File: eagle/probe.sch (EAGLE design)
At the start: 14 parts

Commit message: probe pcb v1
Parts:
- removed LED10, LED11, LED12, LED13, LED14, LED4, LED5, LED6, LED7, LED8, LED9: (no value), led:LED5MM
- added TO1, TO2, TO3, TO4, TO5, TO6: (no value), general:LED5MM
- UV1, UV2, UV3: device led:LED5MM -> general:LED5MM
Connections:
- new net N$2: TO1.C, TO2.C, TO3.C, TO4.C, TO5.C, TO6.C
- net N$1: now also TO1.A, TO2.A, TO3.A, TO4.A, TO5.A, TO6.A
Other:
- moved on the sheet: UV1, UV2, UV3

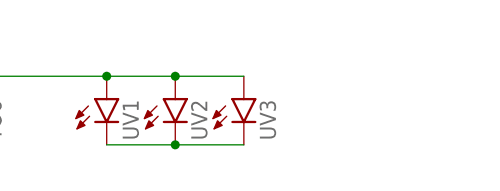
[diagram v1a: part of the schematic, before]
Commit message: Updated probe and rear eagle files
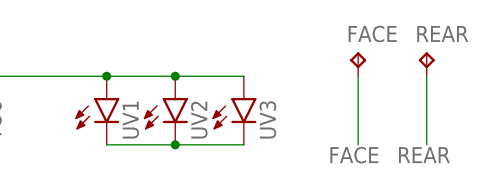
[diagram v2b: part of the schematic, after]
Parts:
- added FACE, REAR: TPTP10R, testpad:TPTP10R
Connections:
- new net FACE: FACE.TP
- new net REAR: REAR.TP
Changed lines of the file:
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@@
 </variantdefs>
 <classes>
-<class number="0" name="default" width="0.2032" drill="0">
+<class number="0" name="default" width="0.1524" drill="0">
+</class>
+<class number="1" name="thick" width="0.508" drill="0">
 </class>
 </classes>
@@
 <part name="UV2" library="general" deviceset="LED" device="5MM" package3d_urn="urn:adsk.eagle:package:15799/2"/>
 <part name="UV3" library="general" deviceset="LED" device="5MM" package3d_urn="urn:adsk.eagle:package:15799/2"/>
+<part name="FACE" library="testpad" library_urn="urn:adsk.eagle:library:385" deviceset="TP" device="TP10R" package3d_urn="urn:adsk.eagle:package:27959/1"/>
+<part name="REAR" library="testpad" library_urn="urn:adsk.eagle:library:385" deviceset="TP" device="TP10R" package3d_urn="urn:adsk.eagle:package:27959/1"/>
 </parts>
 <sheets>
@@
 <attribute name="NAME" x="41.656" y="46.228" size="1.778" layer="95" rot="R90"/>
 <attribute name="VALUE" x="43.815" y="46.228" size="1.778" layer="96" rot="R90"/>
+</instance>
+<instance part="FACE" gate="G$1" x="50.8" y="55.88" smashed="yes">
+<attribute name="NAME" x="49.53" y="57.15" size="1.778" layer="95"/>
+<attribute name="TP_SIGNAL_NAME" x="52.07" y="54.61" size="1.778" layer="97"/>
+</instance>
+<instance part="REAR" gate="G$1" x="58.42" y="55.88" smashed="yes">
+<attribute name="NAME" x="57.15" y="57.15" size="1.778" layer="95"/>
+<attribute name="TP_SIGNAL_NAME" x="59.69" y="54.61" size="1.778" layer="97"/>
 </instance>
 </instances>
@@
 </segment>
 </net>
+<net name="FACE" class="1">
+<segment>
+<pinref part="FACE" gate="G$1" pin="TP"/>
+<wire x1="50.8" y1="53.34" x2="50.8" y2="45.72" width="0.1524" layer="91"/>
+<label x="47.498" y="43.688" size="1.778" layer="95"/>
+</segment>
+</net>
+<net name="REAR" class="0">
+<segment>
+<pinref part="REAR" gate="G$1" pin="TP"/>
+<wire x1="58.42" y1="53.34" x2="58.42" y2="45.72" width="0.1524" layer="91"/>
+<label x="55.118" y="43.688" size="1.778" layer="95"/>
+</segment>
+</net>
 </nets>
 </sheet>
@@
 </drawing>
 <compatibility>
+<note version="8.2" severity="warning">
+Since Version 8.2, EAGLE supports online libraries. The ids
+of those online libraries will not be understood (or retained)
+with this version.
+</note>
 <note version="8.3" severity="warning">
 Since Version 8.3, EAGLE supports URNs for individual library

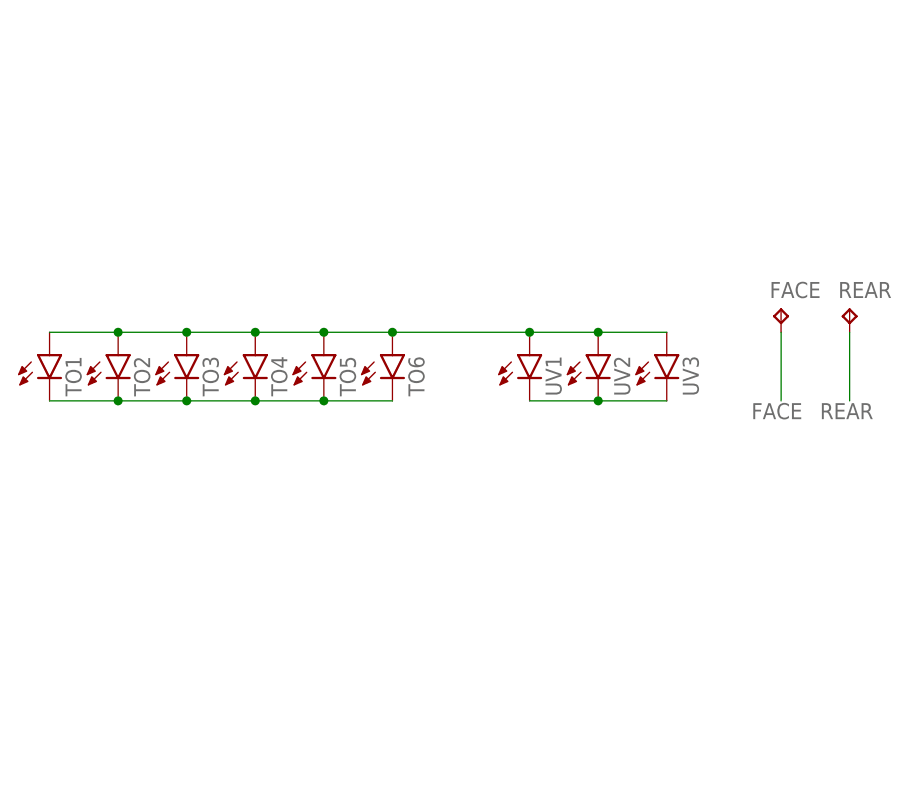
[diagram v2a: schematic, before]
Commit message: Re-organise eagle folder
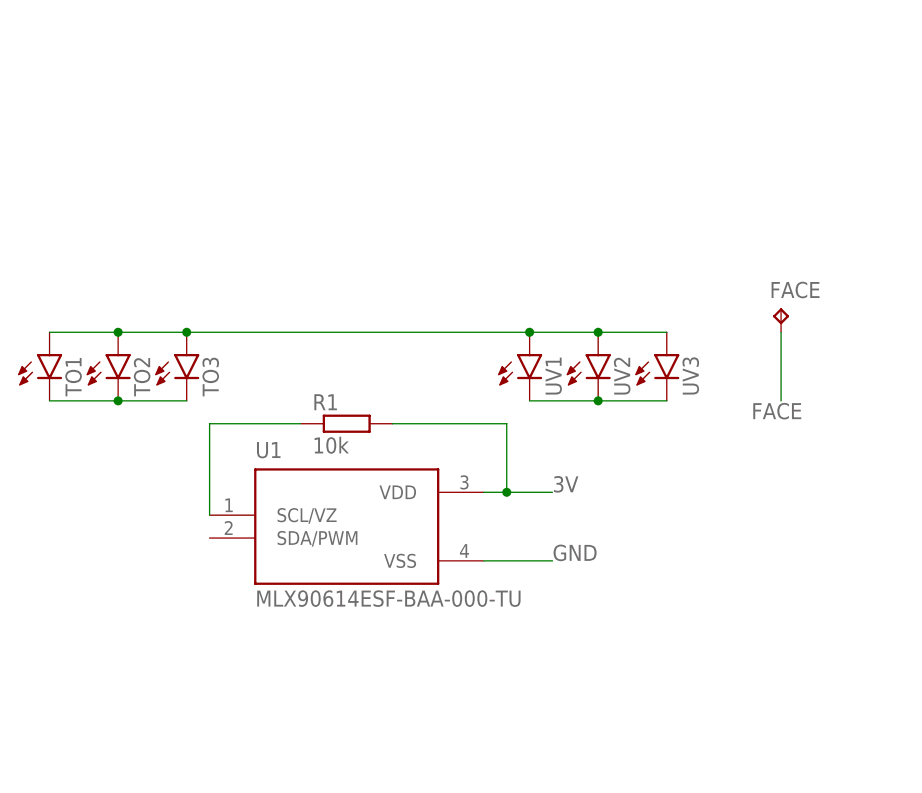
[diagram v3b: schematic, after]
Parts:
- removed REAR: TPTP10R, testpad:TPTP10R
- removed TO4, TO5, TO6: (no value), general:LED5MM
- added R1: 10k, resistor:R-EU_R0805
- added U1: MLX90614ESF-BAA-000-TU, MLX90614ESF-BAA-000-TU:MLX90614ESF-BAA-000-TU
- FACE: value TPTP10R -> TPTP14R; device testpad:TPTP10R -> testpad:TPTP14R
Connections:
- removed net N$1: TO1.A, TO2.A, TO3.A, TO4.A, TO5.A, TO6.A, UV1.A, UV2.A, UV3.A
- removed net REAR: REAR.TP
- new net 3V: R1.2, TO1.A, TO2.A, TO3.A, U1.VDD, UV1.A, UV2.A, UV3.A
- new net GND: U1.VSS
- new net SCL: R1.1, U1.SCL/VZ
- net N$2: no longer TO4.C, TO5.C, TO6.C
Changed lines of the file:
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@@
 </variantdefs>
 <classes>
-<class number="0" name="default" width="0.1524" drill="0">
-</class>
-<class number="1" name="thick" width="0.508" drill="0">
+<class number="0" name="default" width="0" drill="0">
 </class>
 </classes>
@@
 <part name="TO2" library="general" deviceset="LED" device="5MM" package3d_urn="urn:adsk.eagle:package:15799/2"/>
 <part name="TO3" library="general" deviceset="LED" device="5MM" package3d_urn="urn:adsk.eagle:package:15799/2"/>
-<part name="TO4" library="general" deviceset="LED" device="5MM" package3d_urn="urn:adsk.eagle:package:15799/2"/>
-<part name="TO5" library="general" deviceset="LED" device="5MM" package3d_urn="urn:adsk.eagle:package:15799/2"/>
-<part name="TO6" library="general" deviceset="LED" device="5MM" package3d_urn="urn:adsk.eagle:package:15799/2"/>
 <part name="UV1" library="general" deviceset="LED" device="5MM" package3d_urn="urn:adsk.eagle:package:15799/2"/>
 <part name="UV2" library="general" deviceset="LED" device="5MM" package3d_urn="urn:adsk.eagle:package:15799/2"/>
 <part name="UV3" library="general" deviceset="LED" device="5MM" package3d_urn="urn:adsk.eagle:package:15799/2"/>
-<part name="FACE" library="testpad" library_urn="urn:adsk.eagle:library:385" deviceset="TP" device="TP10R" package3d_urn="urn:adsk.eagle:package:27959/1"/>
-<part name="REAR" library="testpad" library_urn="urn:adsk.eagle:library:385" deviceset="TP" device="TP10R" package3d_urn="urn:adsk.eagle:package:27959/1"/>
+<part name="U1" library="MLX90614ESF-BAA-000-TU" deviceset="MLX90614ESF-BAA-000-TU" device=""/>
+<part name="FACE" library="testpad" library_urn="urn:adsk.eagle:library:385" deviceset="TP" device="TP14R" package3d_urn="urn:adsk.eagle:package:27966/1"/>
+<part name="R1" library="resistor" library_urn="urn:adsk.eagle:library:348" deviceset="R-EU_" device="R0805" package3d_urn="urn:adsk.eagle:package:23553/2" value="10k"/>
 </parts>
 <sheets>
@@
 <attribute name="VALUE" x="-9.525" y="46.228" size="1.778" layer="96" rot="R90"/>
 </instance>
-<instance part="TO4" gate="G$1" x="-7.62" y="50.8" smashed="yes">
-<attribute name="NAME" x="-4.064" y="46.228" size="1.778" layer="95" rot="R90"/>
-<attribute name="VALUE" x="-1.905" y="46.228" size="1.778" layer="96" rot="R90"/>
-</instance>
-<instance part="TO5" gate="G$1" x="0" y="50.8" smashed="yes">
-<attribute name="NAME" x="3.556" y="46.228" size="1.778" layer="95" rot="R90"/>
-<attribute name="VALUE" x="5.715" y="46.228" size="1.778" layer="96" rot="R90"/>
-</instance>
-<instance part="TO6" gate="G$1" x="7.62" y="50.8" smashed="yes">
-<attribute name="NAME" x="11.176" y="46.228" size="1.778" layer="95" rot="R90"/>
-<attribute name="VALUE" x="13.335" y="46.228" size="1.778" layer="96" rot="R90"/>
-</instance>
 <instance part="UV1" gate="G$1" x="22.86" y="50.8" smashed="yes">
 <attribute name="NAME" x="26.416" y="46.228" size="1.778" layer="95" rot="R90"/>
@@
 <attribute name="VALUE" x="43.815" y="46.228" size="1.778" layer="96" rot="R90"/>
 </instance>
+<instance part="U1" gate="G$1" x="2.54" y="33.02" smashed="yes">
+<attribute name="NAME" x="-7.62" y="39.37" size="1.778" layer="95"/>
+<attribute name="VALUE" x="-7.62" y="22.86" size="1.778" layer="96"/>
+</instance>
 <instance part="FACE" gate="G$1" x="50.8" y="55.88" smashed="yes">
 <attribute name="NAME" x="49.53" y="57.15" size="1.778" layer="95"/>
 <attribute name="TP_SIGNAL_NAME" x="52.07" y="54.61" size="1.778" layer="97"/>
 </instance>
-<instance part="REAR" gate="G$1" x="58.42" y="55.88" smashed="yes">
-<attribute name="NAME" x="57.15" y="57.15" size="1.778" layer="95"/>
-<attribute name="TP_SIGNAL_NAME" x="59.69" y="54.61" size="1.778" layer="97"/>
+<instance part="R1" gate="G$1" x="2.54" y="43.18" smashed="yes">
+<attribute name="NAME" x="-1.27" y="44.6786" size="1.778" layer="95"/>
+<attribute name="VALUE" x="-1.27" y="39.878" size="1.778" layer="96"/>
 </instance>
 </instances>
@@
 </busses>
 <nets>
-<net name="N$1" class="0">
-<segment>
-<pinref part="TO1" gate="G$1" pin="A"/>
-<pinref part="TO2" gate="G$1" pin="A"/>
-<wire x1="-30.48" y1="53.34" x2="-22.86" y2="53.34" width="0.1524" layer="91"/>
-<pinref part="TO3" gate="G$1" pin="A"/>
-<wire x1="-22.86" y1="53.34" x2="-15.24" y2="53.34" width="0.1524" layer="91"/>
-<junction x="-22.86" y="53.34"/>
-<pinref part="TO4" gate="G$1" pin="A"/>
-<wire x1="-15.24" y1="53.34" x2="-7.62" y2="53.34" width="0.1524" layer="91"/>
-<junction x="-15.24" y="53.34"/>
-<pinref part="TO5" gate="G$1" pin="A"/>
-<wire x1="-7.62" y1="53.34" x2="0" y2="53.34" width="0.1524" layer="91"/>
-<junction x="-7.62" y="53.34"/>
-<pinref part="TO6" gate="G$1" pin="A"/>
-<wire x1="0" y1="53.34" x2="7.62" y2="53.34" width="0.1524" layer="91"/>
-<junction x="0" y="53.34"/>
-<pinref part="UV1" gate="G$1" pin="A"/>
-<pinref part="UV2" gate="G$1" pin="A"/>
-<wire x1="22.86" y1="53.34" x2="30.48" y2="53.34" width="0.1524" layer="91"/>
-<pinref part="UV3" gate="G$1" pin="A"/>
-<wire x1="30.48" y1="53.34" x2="38.1" y2="53.34" width="0.1524" layer="91"/>
-<junction x="30.48" y="53.34"/>
-<wire x1="7.62" y1="53.34" x2="22.86" y2="53.34" width="0.1524" layer="91"/>
-<junction x="7.62" y="53.34"/>
-<junction x="22.86" y="53.34"/>
-</segment>
-</net>
 <net name="N$2" class="0">
 <segment>
@@
 <wire x1="-22.86" y1="45.72" x2="-15.24" y2="45.72" width="0.1524" layer="91"/>
 <junction x="-22.86" y="45.72"/>
-<pinref part="TO4" gate="G$1" pin="C"/>
-<wire x1="-15.24" y1="45.72" x2="-7.62" y2="45.72" width="0.1524" layer="91"/>
-<junction x="-15.24" y="45.72"/>
-<pinref part="TO5" gate="G$1" pin="C"/>
-<wire x1="-7.62" y1="45.72" x2="0" y2="45.72" width="0.1524" layer="91"/>
-<junction x="-7.62" y="45.72"/>
-<pinref part="TO6" gate="G$1" pin="C"/>
-<wire x1="0" y1="45.72" x2="7.62" y2="45.72" width="0.1524" layer="91"/>
-<junction x="0" y="45.72"/>
 </segment>
 </net>
@@
 </segment>
 </net>
-<net name="FACE" class="1">
+<net name="FACE" class="0">
 <segment>
-<pinref part="FACE" gate="G$1" pin="TP"/>
 <wire x1="50.8" y1="53.34" x2="50.8" y2="45.72" width="0.1524" layer="91"/>
 <label x="47.498" y="43.688" size="1.778" layer="95"/>
+<pinref part="FACE" gate="G$1" pin="TP"/>
 </segment>
 </net>
-<net name="REAR" class="0">
+<net name="GND" class="0">
 <segment>
-<pinref part="REAR" gate="G$1" pin="TP"/>
-<wire x1="58.42" y1="53.34" x2="58.42" y2="45.72" width="0.1524" layer="91"/>
-<label x="55.118" y="43.688" size="1.778" layer="95"/>
+<pinref part="U1" gate="G$1" pin="VSS"/>
+<wire x1="17.78" y1="27.94" x2="25.4" y2="27.94" width="0.1524" layer="91"/>
+<label x="25.4" y="27.94" size="1.778" layer="95"/>
 </segment>
 </net>
+<net name="3V" class="0">
+<segment>
+<pinref part="U1" gate="G$1" pin="VDD"/>
+<wire x1="17.78" y1="35.56" x2="20.32" y2="35.56" width="0.1524" layer="91"/>
+<label x="25.4" y="35.56" size="1.778" layer="95"/>
+<pinref part="R1" gate="G$1" pin="2"/>
+<wire x1="20.32" y1="35.56" x2="25.4" y2="35.56" width="0.1524" layer="91"/>
+<wire x1="7.62" y1="43.18" x2="20.32" y2="43.18" width="0.1524" layer="91"/>
+<wire x1="20.32" y1="43.18" x2="20.32" y2="35.56" width="0.1524" layer="91"/>
+<junction x="20.32" y="35.56"/>
+</segment>
+<segment>
+<pinref part="TO1" gate="G$1" pin="A"/>
+<pinref part="TO2" gate="G$1" pin="A"/>
+<wire x1="-30.48" y1="53.34" x2="-22.86" y2="53.34" width="0.1524" layer="91"/>
+<pinref part="TO3" gate="G$1" pin="A"/>
+<wire x1="-22.86" y1="53.34" x2="-15.24" y2="53.34" width="0.1524" layer="91"/>
+<junction x="-22.86" y="53.34"/>
+<junction x="-15.24" y="53.34"/>
+<pinref part="UV1" gate="G$1" pin="A"/>
+<pinref part="UV2" gate="G$1" pin="A"/>
+<wire x1="22.86" y1="53.34" x2="30.48" y2="53.34" width="0.1524" layer="91"/>
+<pinref part="UV3" gate="G$1" pin="A"/>
+<wire x1="30.48" y1="53.34" x2="38.1" y2="53.34" width="0.1524" layer="91"/>
+<junction x="30.48" y="53.34"/>
+<wire x1="-15.24" y1="53.34" x2="22.86" y2="53.34" width="0.1524" layer="91"/>
+<junction x="22.86" y="53.34"/>
+</segment>
+</net>
+<net name="SCL" class="0">
+<segment>
+<pinref part="U1" gate="G$1" pin="SCL/VZ"/>
+<wire x1="-12.7" y1="33.02" x2="-12.7" y2="43.18" width="0.1524" layer="91"/>
+<pinref part="R1" gate="G$1" pin="1"/>
+<wire x1="-12.7" y1="43.18" x2="-2.54" y2="43.18" width="0.1524" layer="91"/>
+</segment>
+</net>

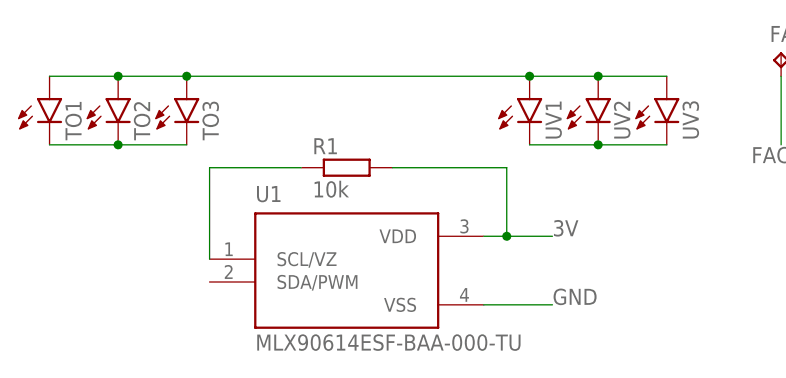
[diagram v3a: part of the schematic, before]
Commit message: First order of probe, probebase and FFC breakout PCBs for 22mm enclosure
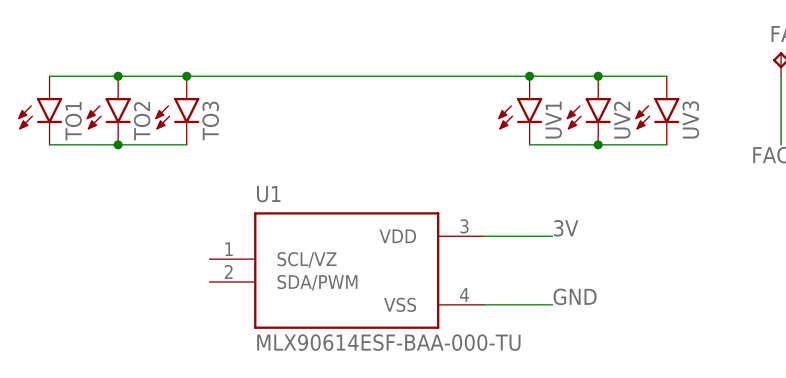
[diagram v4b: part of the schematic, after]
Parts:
- removed R1: 10k, resistor:R-EU_R0805
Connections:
- removed net SCL: R1.1, U1.SCL/VZ
- net 3V: no longer R1.2
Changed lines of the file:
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@@
 <part name="U1" library="MLX90614ESF-BAA-000-TU" deviceset="MLX90614ESF-BAA-000-TU" device=""/>
 <part name="FACE" library="testpad" library_urn="urn:adsk.eagle:library:385" deviceset="TP" device="TP14R" package3d_urn="urn:adsk.eagle:package:27966/1"/>
-<part name="R1" library="resistor" library_urn="urn:adsk.eagle:library:348" deviceset="R-EU_" device="R0805" package3d_urn="urn:adsk.eagle:package:23553/2" value="10k"/>
 </parts>
 <sheets>
@@
 <attribute name="NAME" x="49.53" y="57.15" size="1.778" layer="95"/>
 <attribute name="TP_SIGNAL_NAME" x="52.07" y="54.61" size="1.778" layer="97"/>
-</instance>
-<instance part="R1" gate="G$1" x="2.54" y="43.18" smashed="yes">
-<attribute name="NAME" x="-1.27" y="44.6786" size="1.778" layer="95"/>
-<attribute name="VALUE" x="-1.27" y="39.878" size="1.778" layer="96"/>
 </instance>
 </instances>
@@
 <segment>
 <pinref part="U1" gate="G$1" pin="VDD"/>
-<wire x1="17.78" y1="35.56" x2="20.32" y2="35.56" width="0.1524" layer="91"/>
 <label x="25.4" y="35.56" size="1.778" layer="95"/>
-<pinref part="R1" gate="G$1" pin="2"/>
-<wire x1="20.32" y1="35.56" x2="25.4" y2="35.56" width="0.1524" layer="91"/>
-<wire x1="7.62" y1="43.18" x2="20.32" y2="43.18" width="0.1524" layer="91"/>
-<wire x1="20.32" y1="43.18" x2="20.32" y2="35.56" width="0.1524" layer="91"/>
-<junction x="20.32" y="35.56"/>
+<wire x1="17.78" y1="35.56" x2="25.4" y2="35.56" width="0.1524" layer="91"/>
 </segment>
 <segment>
@@
 </segment>
 </net>
-<net name="SCL" class="0">
-<segment>
-<pinref part="U1" gate="G$1" pin="SCL/VZ"/>
-<wire x1="-12.7" y1="33.02" x2="-12.7" y2="43.18" width="0.1524" layer="91"/>
-<pinref part="R1" gate="G$1" pin="1"/>
-<wire x1="-12.7" y1="43.18" x2="-2.54" y2="43.18" width="0.1524" layer="91"/>
-</segment>
-</net>
